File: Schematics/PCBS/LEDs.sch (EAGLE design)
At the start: 17 parts, among them IC1 ATMEGA328P-AU, Q1 TRANSISTOR-FET_DMN2004K, Q2 TRANSISTOR-FET_DMN2004K, Q3 TRANSISTOR-FET_DMN2004K, Q4 TRANSISTOR-FET_DMN2004K, Q5 TRANSISTOR-FET_DMN2004K, Q6 TRANSISTOR-FET_DMN2004K, Q7 TRANSISTOR-FET_DMN2004K, Q8 TRANSISTOR-FET_DMN2004K, Q9 TRANSISTOR-FET_DMN2004K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

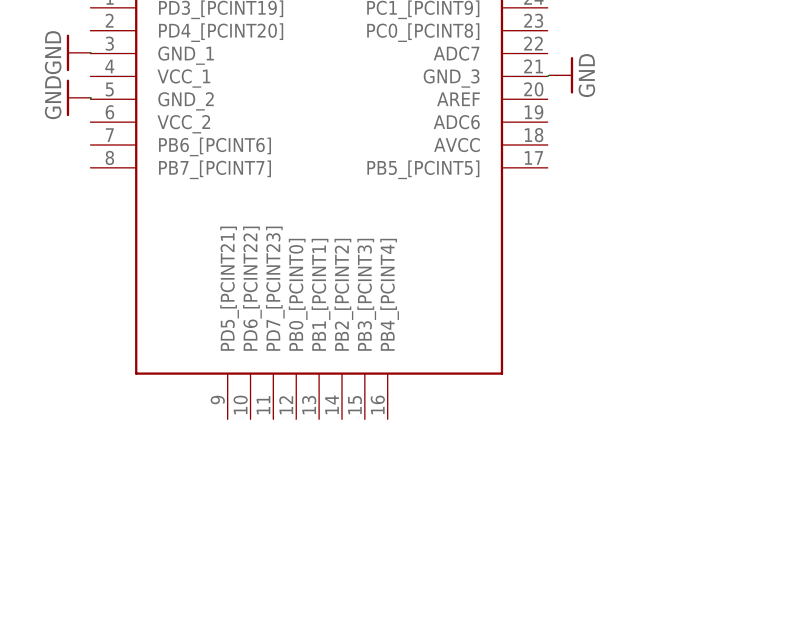
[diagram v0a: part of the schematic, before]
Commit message: join Led To IC
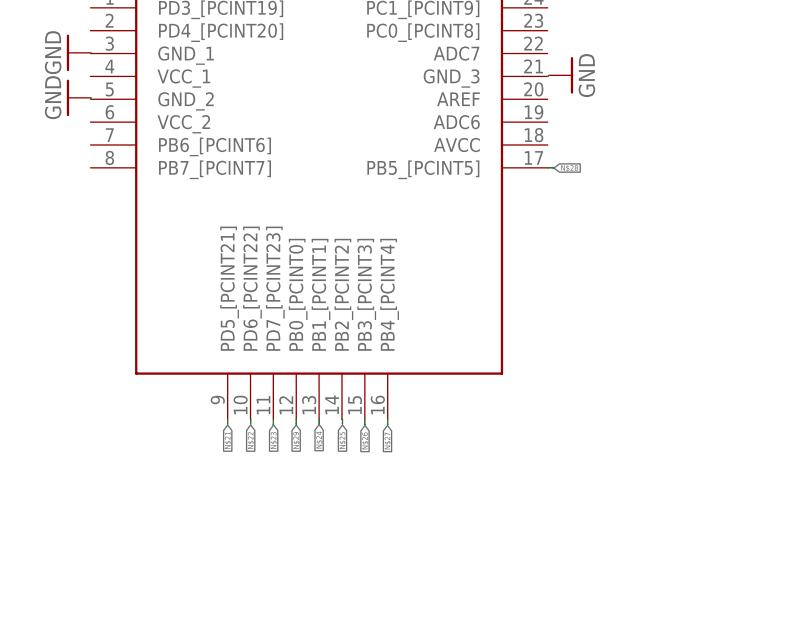
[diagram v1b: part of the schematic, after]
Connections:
- new net N$21: IC1.PD5_[PCINT21]
- new net N$22: IC1.PD6_[PCINT22]
- new net N$23: IC1.PD7_[PCINT23]
- new net N$24: IC1.PB1_[PCINT1]
- new net N$25: IC1.PB2_[PCINT2]
- new net N$26: IC1.PB3_[PCINT3]
- new net N$27: IC1.PB4_[PCINT4]
- new net N$28: IC1.PB5_[PCINT5]
- new net N$29: IC1.PB0_[PCINT0]
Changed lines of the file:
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@@
 <setting verticaltext="up"/>
 </settings>
-<grid distance="0.5" unitdist="mm" unit="mm" style="lines" multiple="1" display="yes" altdistance="0.0003125" altunitdist="mm" altunit="mm"/>
+<grid distance="0.05" unitdist="mm" unit="mm" style="lines" multiple="1" display="yes" altdistance="0.003125" altunitdist="mic" altunit="mm"/>
 <layers>
 <layer number="1" name="Top" color="4" fill="1" visible="no" active="no"/>
@@
 </segment>
 </net>
+<net name="N$21" class="0">
+<segment>
+<pinref part="IC1" gate="G$1" pin="PD5_[PCINT21]"/>
+<wire x1="556.24" y1="-68.72" x2="556.24" y2="-69.28" width="0.1524" layer="91"/>
+<label x="556.25" y="-69.35" size="0.6096" layer="95" rot="R270" xref="yes"/>
+</segment>
+</net>
+<net name="N$22" class="0">
+<segment>
+<pinref part="IC1" gate="G$1" pin="PD6_[PCINT22]"/>
+<wire x1="558.78" y1="-68.72" x2="558.8" y2="-68.72" width="0.1524" layer="91"/>
+<wire x1="558.8" y1="-68.72" x2="558.8" y2="-69.28" width="0.1524" layer="91"/>
+<label x="558.8" y="-69.35" size="0.6096" layer="95" rot="R270" xref="yes"/>
+</segment>
+</net>
+<net name="N$23" class="0">
+<segment>
+<pinref part="IC1" gate="G$1" pin="PD7_[PCINT23]"/>
+<wire x1="561.32" y1="-68.72" x2="561.32" y2="-69.3" width="0.1524" layer="91"/>
+<wire x1="561.32" y1="-69.3" x2="561.3" y2="-69.3" width="0.1524" layer="91"/>
+<label x="561.35" y="-69.35" size="0.6096" layer="95" rot="R270" xref="yes"/>
+</segment>
+</net>
+<net name="N$24" class="0">
+<segment>
+<pinref part="IC1" gate="G$1" pin="PB1_[PCINT1]"/>
+<wire x1="566.4" y1="-68.72" x2="566.4" y2="-69.3" width="0.1524" layer="91"/>
+<label x="566.4" y="-69.3" size="0.6096" layer="95" rot="R270" xref="yes"/>
+</segment>
+</net>
+<net name="N$25" class="0">
+<segment>
+<pinref part="IC1" gate="G$1" pin="PB2_[PCINT2]"/>
+<wire x1="568.94" y1="-68.72" x2="569" y2="-68.72" width="0.1524" layer="91"/>
+<wire x1="569" y1="-68.72" x2="569" y2="-69.25" width="0.1524" layer="91"/>
+<label x="569" y="-69.35" size="0.6096" layer="95" rot="R270" xref="yes"/>
+</segment>
+</net>
+<net name="N$26" class="0">
+<segment>
+<pinref part="IC1" gate="G$1" pin="PB3_[PCINT3]"/>
+<wire x1="571.48" y1="-68.72" x2="571.48" y2="-69.3" width="0.1524" layer="91"/>
+<wire x1="571.48" y1="-69.3" x2="571.5" y2="-69.3" width="0.1524" layer="91"/>
+<label x="571.5" y="-69.4" size="0.6096" layer="95" rot="R270" xref="yes"/>
+</segment>
+</net>
+<net name="N$27" class="0">
+<segment>
+<pinref part="IC1" gate="G$1" pin="PB4_[PCINT4]"/>
+<wire x1="574.02" y1="-68.72" x2="574.02" y2="-69.3" width="0.1524" layer="91"/>
+<wire x1="574.02" y1="-69.3" x2="574" y2="-69.3" width="0.1524" layer="91"/>
+<label x="574" y="-69.4" size="0.6096" layer="95" rot="R270" xref="yes"/>
+</segment>
+</net>
+<net name="N$28" class="0">
+<segment>
+<pinref part="IC1" gate="G$1" pin="PB5_[PCINT5]"/>
+<wire x1="592.45" y1="-40.85" x2="592.45" y2="-40.78" width="0.1524" layer="91"/>
+<wire x1="592.45" y1="-40.78" x2="591.8" y2="-40.78" width="0.1524" layer="91"/>
+<label x="592.5" y="-40.8" size="0.6096" layer="95" xref="yes"/>
+</segment>
+</net>
+<net name="N$29" class="0">
+<segment>
+<pinref part="IC1" gate="G$1" pin="PB0_[PCINT0]"/>
+<wire x1="563.86" y1="-68.72" x2="563.86" y2="-69.25" width="0.1524" layer="91"/>
+<wire x1="563.86" y1="-69.25" x2="563.85" y2="-69.25" width="0.1524" layer="91"/>
+<label x="563.85" y="-69.35" size="0.6096" layer="95" rot="R270" xref="yes"/>
+</segment>
+</net>

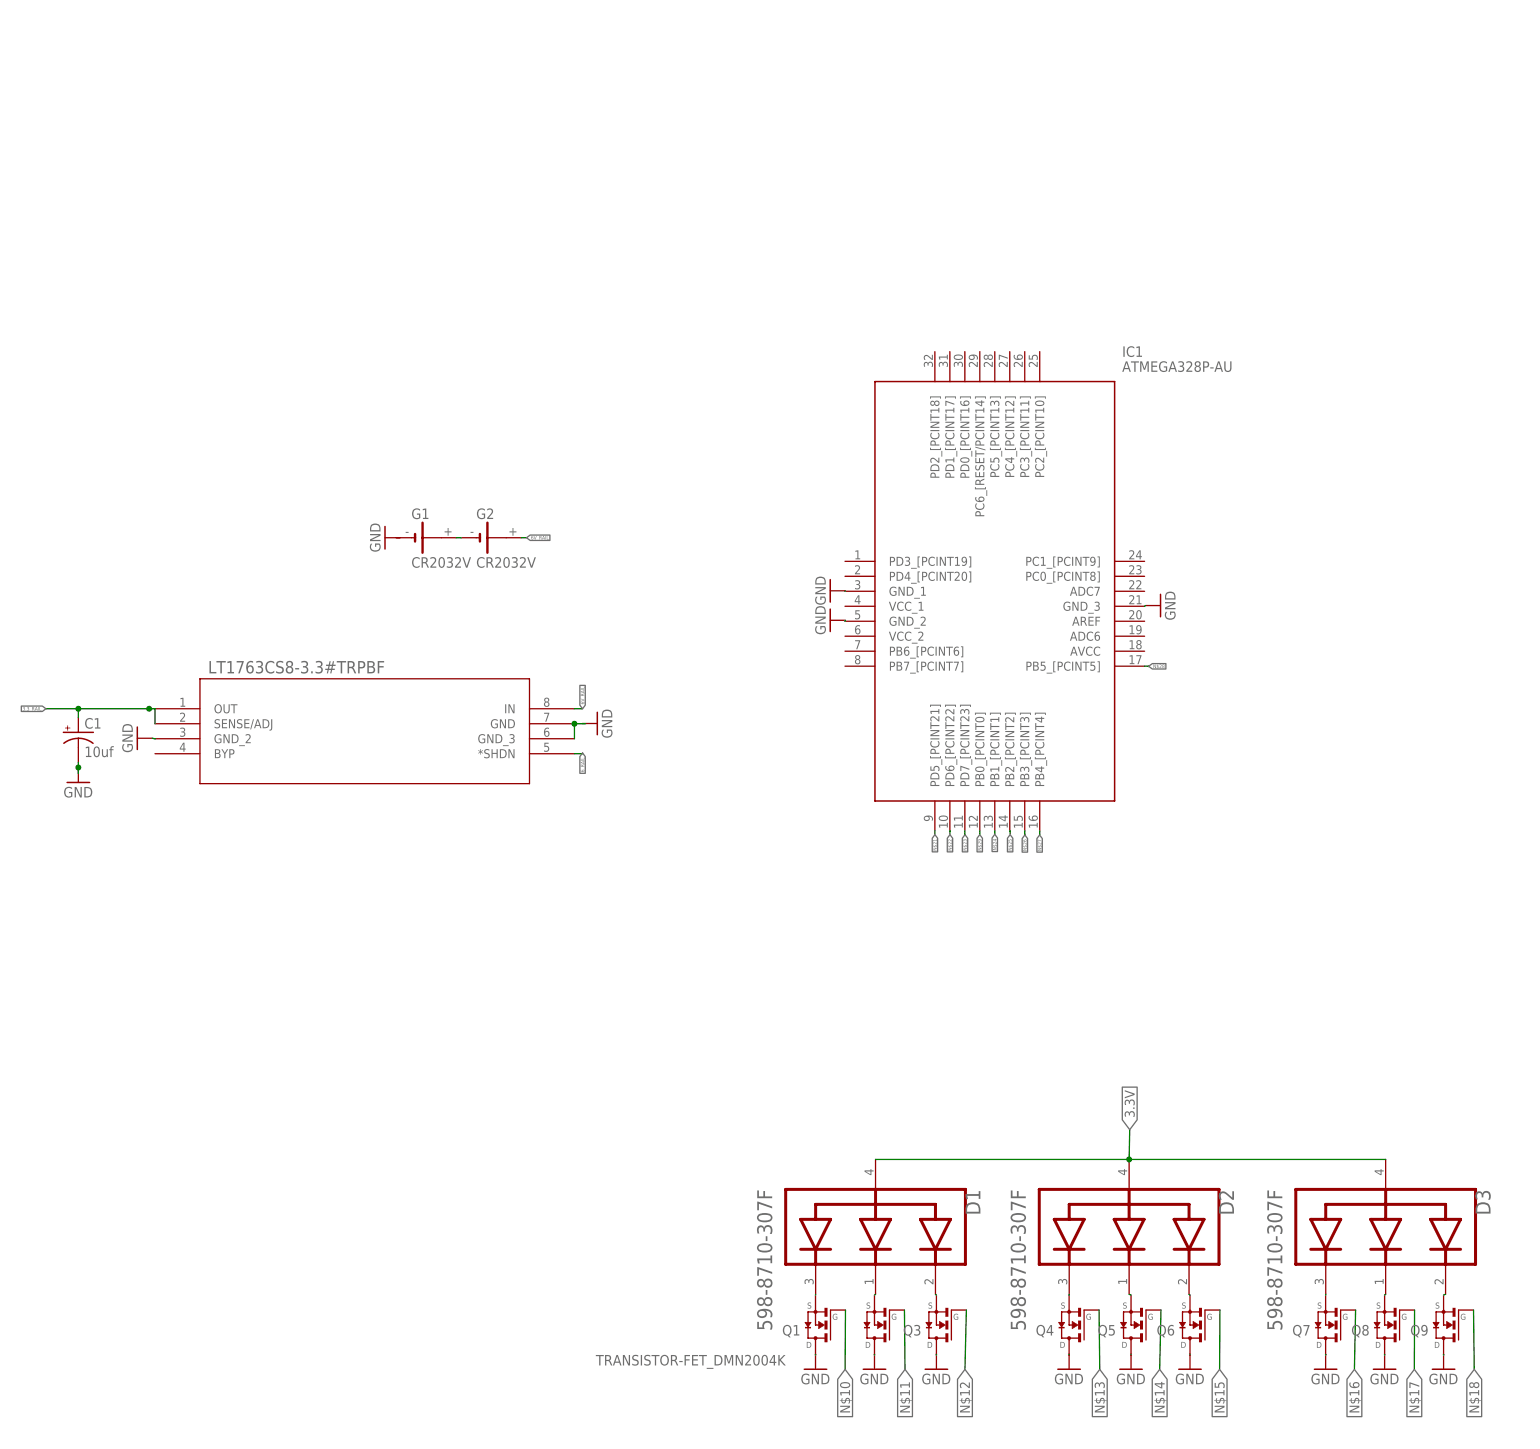
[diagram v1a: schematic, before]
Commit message: connected LED Mosfets to IC + Add headers
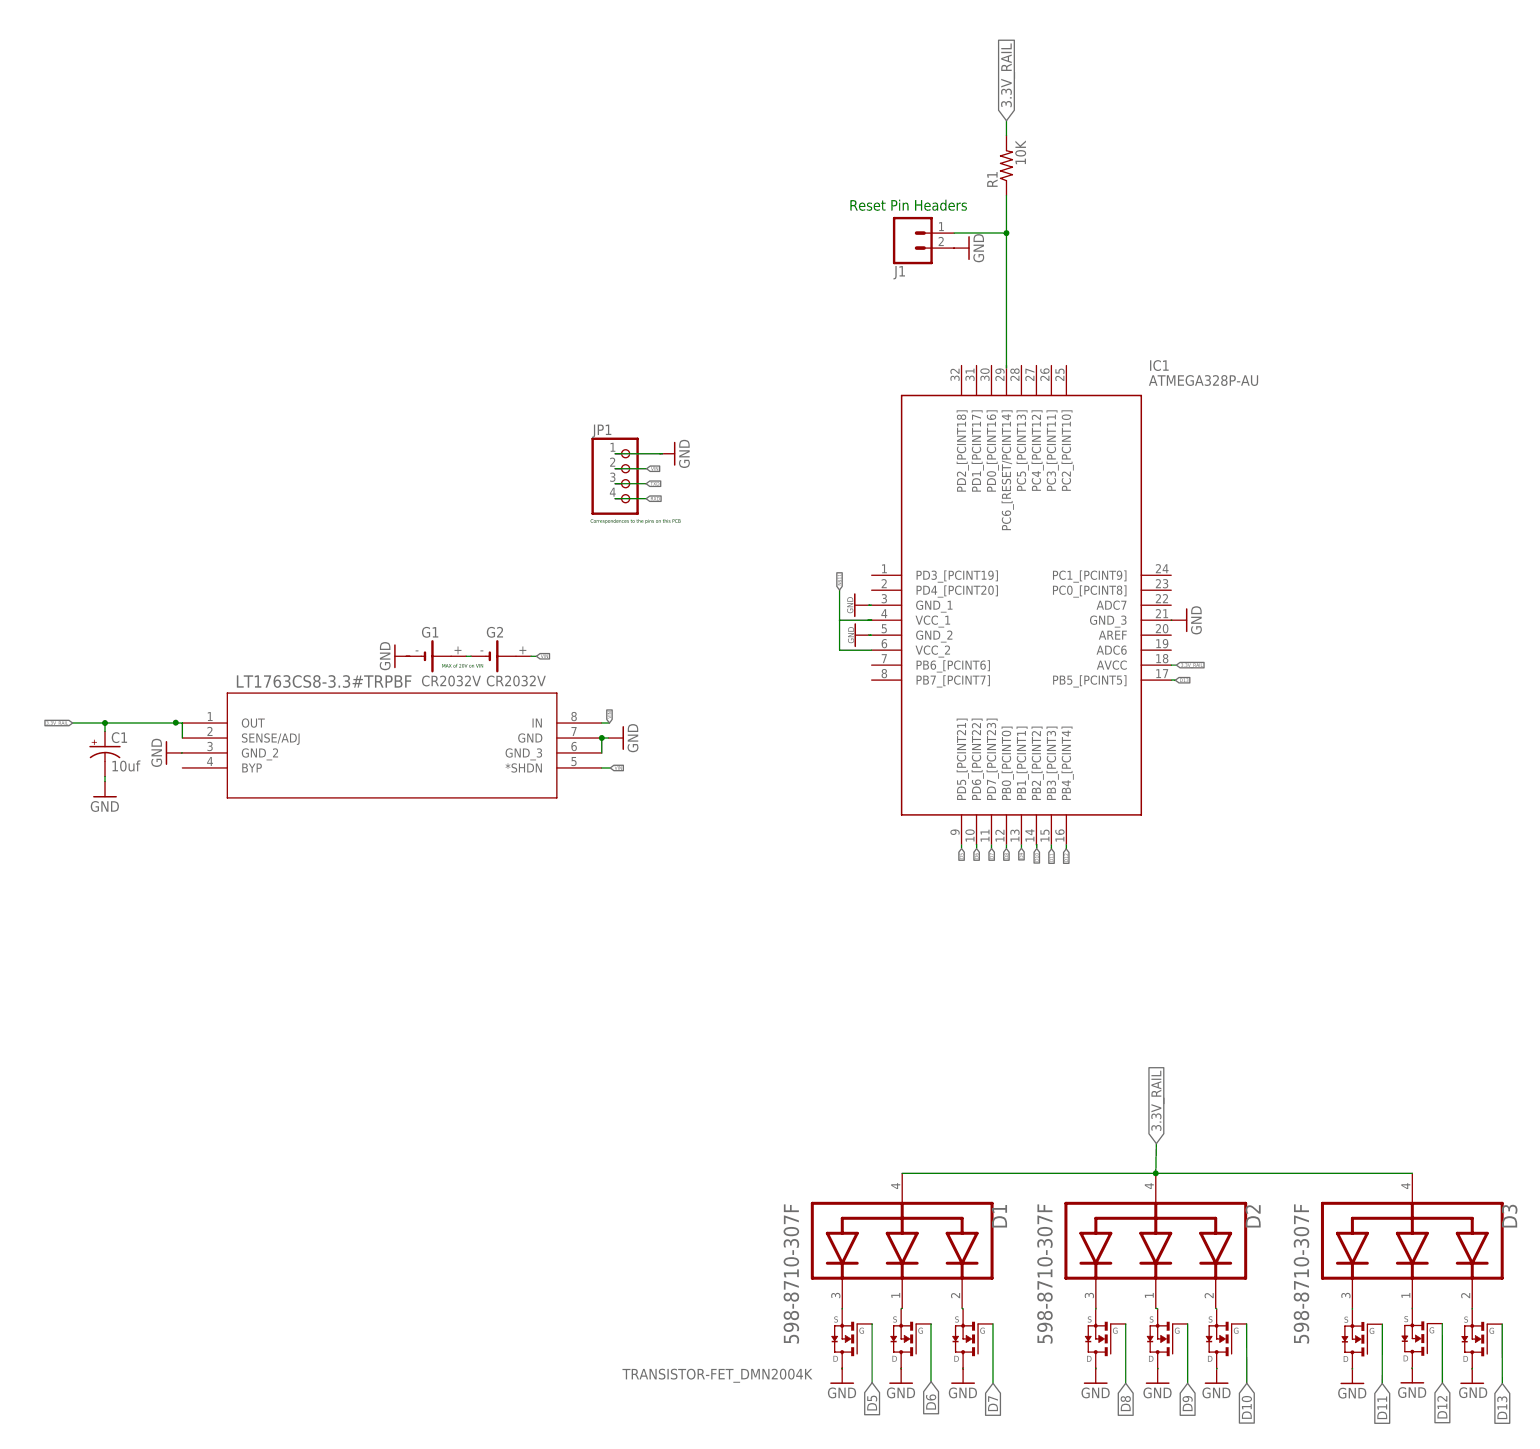
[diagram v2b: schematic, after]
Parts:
- added J1: (no value), SparkFun-Connectors:CONN_02
- added JP1: (no value), pinhead:PINHD-1X4
- added R1: 10K, adafruit:R-US_0207/10
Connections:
- removed net 3.3V: D1.COMMON_ANODE, D2.COMMON_ANODE, D3.COMMON_ANODE
- removed net 3.3_RAIL: C1.+, U1.OUT, U1.SENSE/ADJ
- removed net 6V_RAIL: G2.+, U1.IN
- removed net 6_RAIL: U1.*SHDN
- removed net N$11: Q2.G
- removed net N$12: Q3.G
- removed net N$13: Q4.G
- removed net N$14: Q5.G
- removed net N$16: Q7.G
- removed net N$17: Q8.G
- removed net N$18: Q9.G
- removed net N$20: U1.GND, U1.GND_3
- removed net N$21: IC1.PD5_[PCINT21]
- removed net N$22: IC1.PD6_[PCINT22]
- removed net N$23: IC1.PD7_[PCINT23]
- removed net N$24: IC1.PB1_[PCINT1]
- removed net N$25: IC1.PB2_[PCINT2]
- removed net N$26: IC1.PB3_[PCINT3]
- removed net N$27: IC1.PB4_[PCINT4]
- removed net N$28: IC1.PB5_[PCINT5]
- removed net N$29: IC1.PB0_[PCINT0]
- new net 3.3V_RAIL: C1.+, D1.COMMON_ANODE, D2.COMMON_ANODE, D3.COMMON_ANODE, IC1.AVCC, IC1.VCC_1, R1.2, U1.OUT, U1.SENSE/ADJ
- new net D10: IC1.PB2_[PCINT2], Q6.G
- new net D11: IC1.PB3_[PCINT3], Q7.G
- new net D12: IC1.PB4_[PCINT4], Q8.G
- new net D13: IC1.PB5_[PCINT5], Q9.G
- new net D5: IC1.PD5_[PCINT21], Q1.G
- new net D6: IC1.PD6_[PCINT22], Q2.G
- new net D7: IC1.PD7_[PCINT23], Q3.G
- new net D8: IC1.PB0_[PCINT0], Q4.G
- new net D9: IC1.PB1_[PCINT1], Q5.G
- new net RXD: JP1.4
- new net TXD: JP1.3
- new net VIN: G2.+, JP1.2, U1.*SHDN, U1.IN
- net GND: now also J1.2, JP1.1, U1.GND, U1.GND_3
- net N$10: now also IC1.VCC_2; no longer Q1.G
- net N$15: now also IC1.PC6_[RESET/PCINT14], J1.1, R1.1; no longer Q6.G
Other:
- note added: "Correspondences to the pins on this PCB"
- note added: "MAX of 20V on VIN"
- note added: "Reset Pin Headers"
- moved on the sheet: C1, D1, D2, D3, G1, G2, IC1

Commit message: Fix layout issues via fix to grid
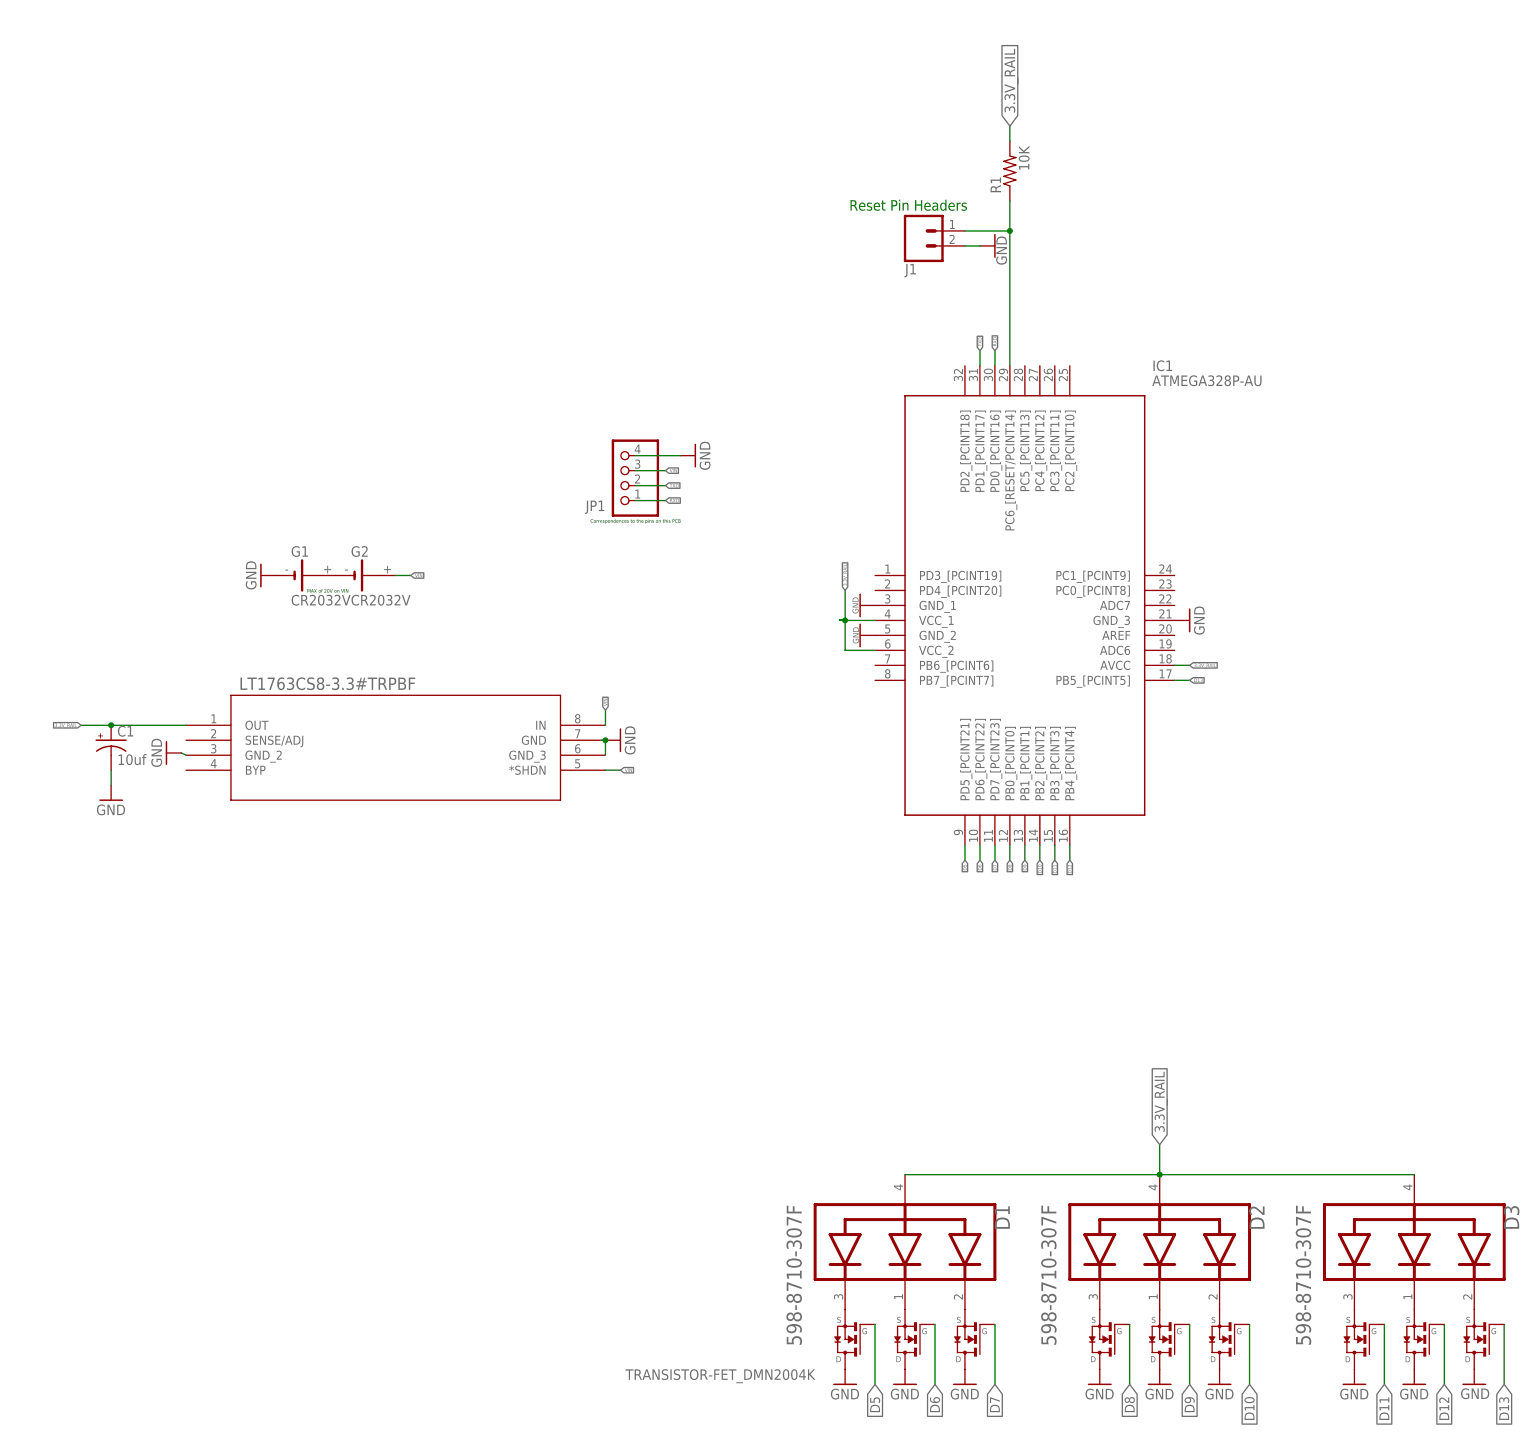
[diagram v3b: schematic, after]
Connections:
- removed net N$10: IC1.VCC_2
- net 3.3V_RAIL: now also IC1.VCC_2; no longer U1.SENSE/ADJ
- net GND: now also G1.-, JP1.4; no longer JP1.1
- net RXD: now also IC1.PD0_[PCINT16], JP1.1; no longer JP1.4
- net TXD: now also IC1.PD1_[PCINT17], JP1.2; no longer JP1.3
- net VIN: now also JP1.3; no longer JP1.2
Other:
- moved on the sheet: C1, D1, D2, G1, G2, IC1, J1, JP1, R1
